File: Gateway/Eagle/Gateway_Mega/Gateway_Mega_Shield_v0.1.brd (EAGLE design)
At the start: 101.6 x 53.3 mm, 10 parts

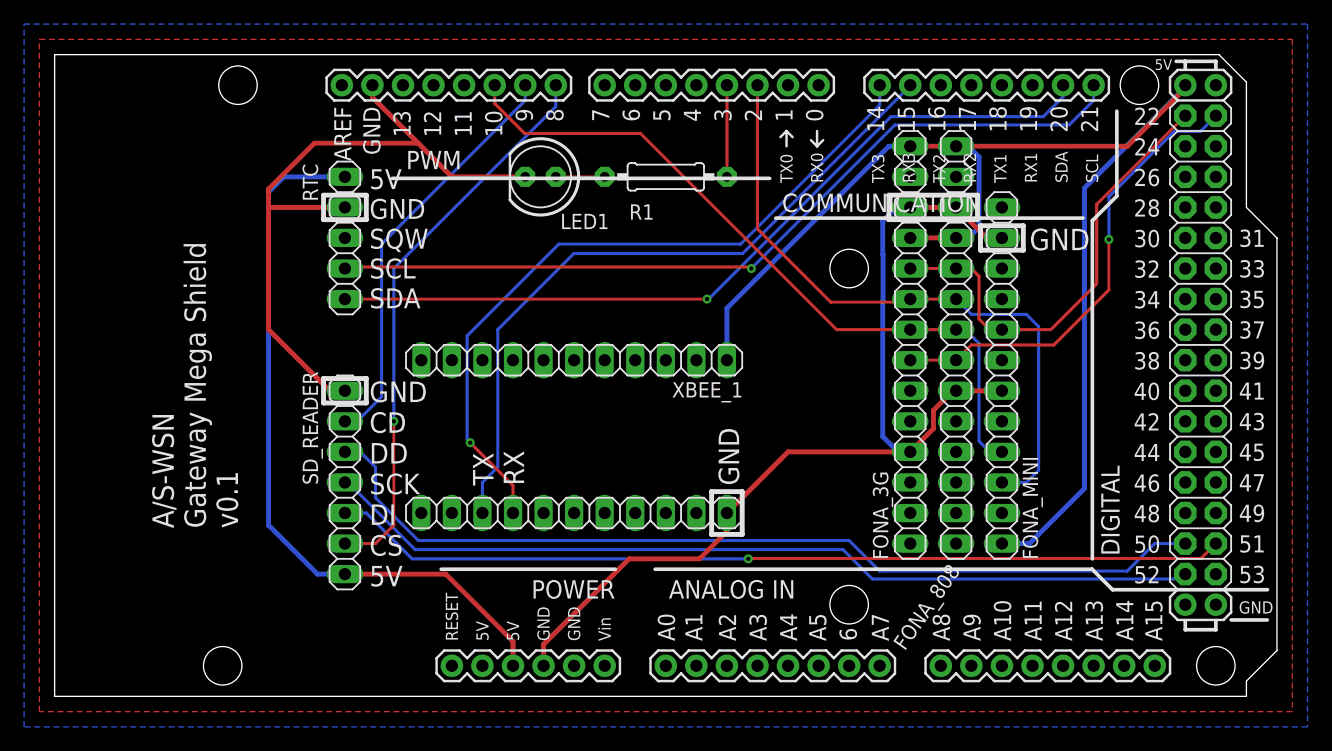
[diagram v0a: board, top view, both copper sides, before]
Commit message: Modify sparkfun arduino mega shield
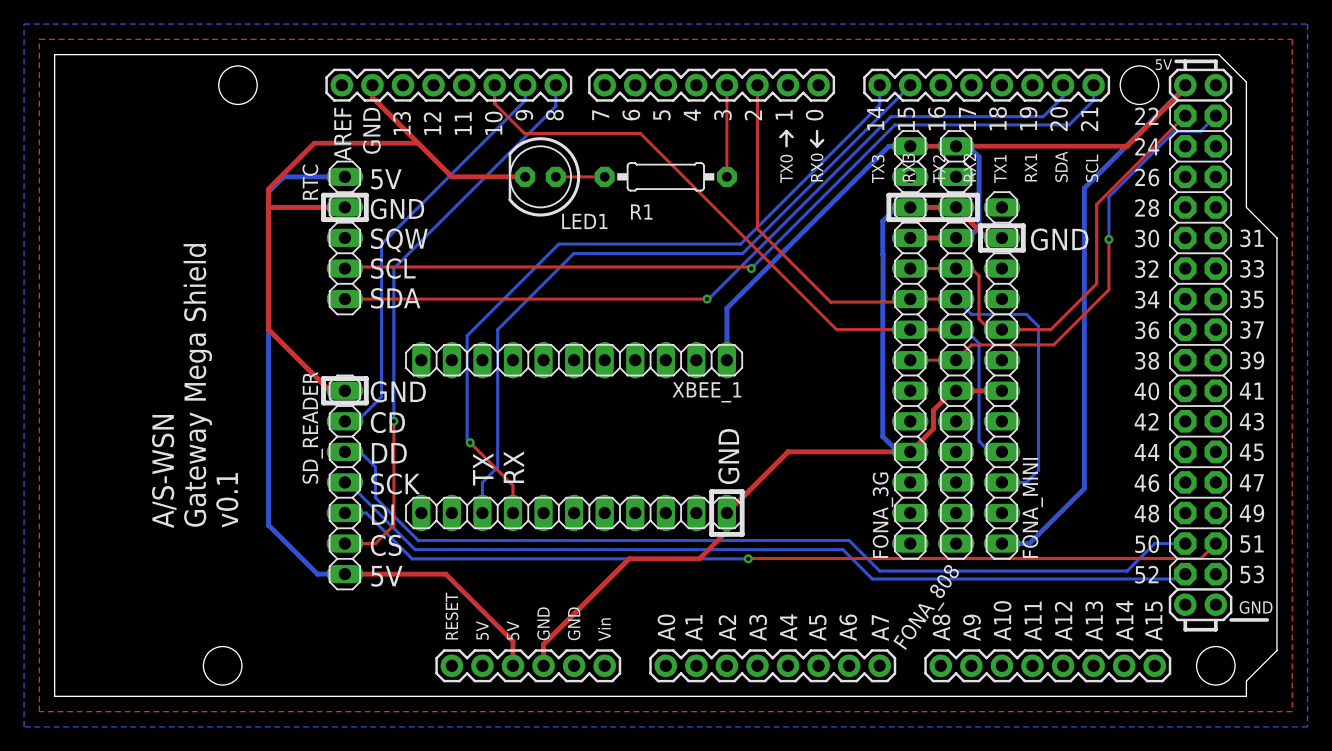
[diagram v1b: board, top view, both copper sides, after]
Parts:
- B1: value ARDUINO_MEGA_R3FULL -> ARDUINO_MEGA_R3_SPARKFUN_MODIFIEDFULL; device SparkFun-Boards:ARDUINO_MEGA -> wsn_x:ARDUINO_MEGA_SPARKFUN_MODIFIED
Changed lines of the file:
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@@
 </autorouter>
 <elements>
-<element name="B1" library="SparkFun-Boards" library_urn="urn:adsk.eagle:library:509" package="ARDUINO_MEGA" package3d_urn="urn:adsk.eagle:package:37320/1" value="ARDUINO_MEGA_R3FULL" x="49.53" y="26.67" smashed="yes"/>
+<element name="B1" library="wsn_x" package="ARDUINO_MEGA_SPARKFUN_MODIFIED" value="ARDUINO_MEGA_R3_SPARKFUN_MODIFIEDFULL" x="49.53" y="26.67" smashed="yes"/>
 <element name="FONA_3G" library="pinhead" library_urn="urn:adsk.eagle:library:325" package="1X14" package3d_urn="urn:adsk.eagle:package:22417/2" value="" x="71.12" y="29.21" smashed="yes" rot="R90">
 <attribute name="NAME" x="69.2912" y="11.3538" size="1.27" layer="25" ratio="10" rot="R90"/>
